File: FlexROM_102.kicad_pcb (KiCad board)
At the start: 2 copper layers, 16.5 x 34.3 mm, 7 parts, among them J1 27C256 DIP LEGS, U1 28C256

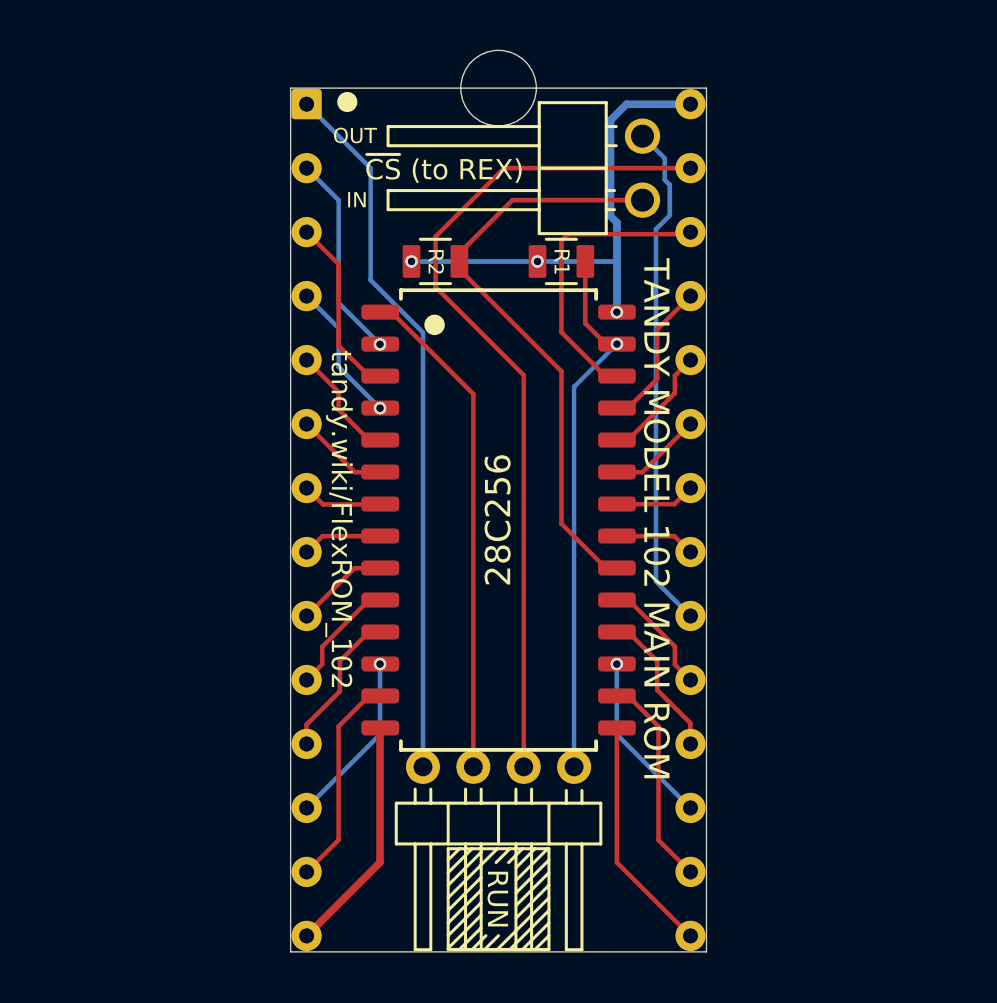
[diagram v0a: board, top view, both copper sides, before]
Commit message: add model 100 optrom programming adapter. readme and renders
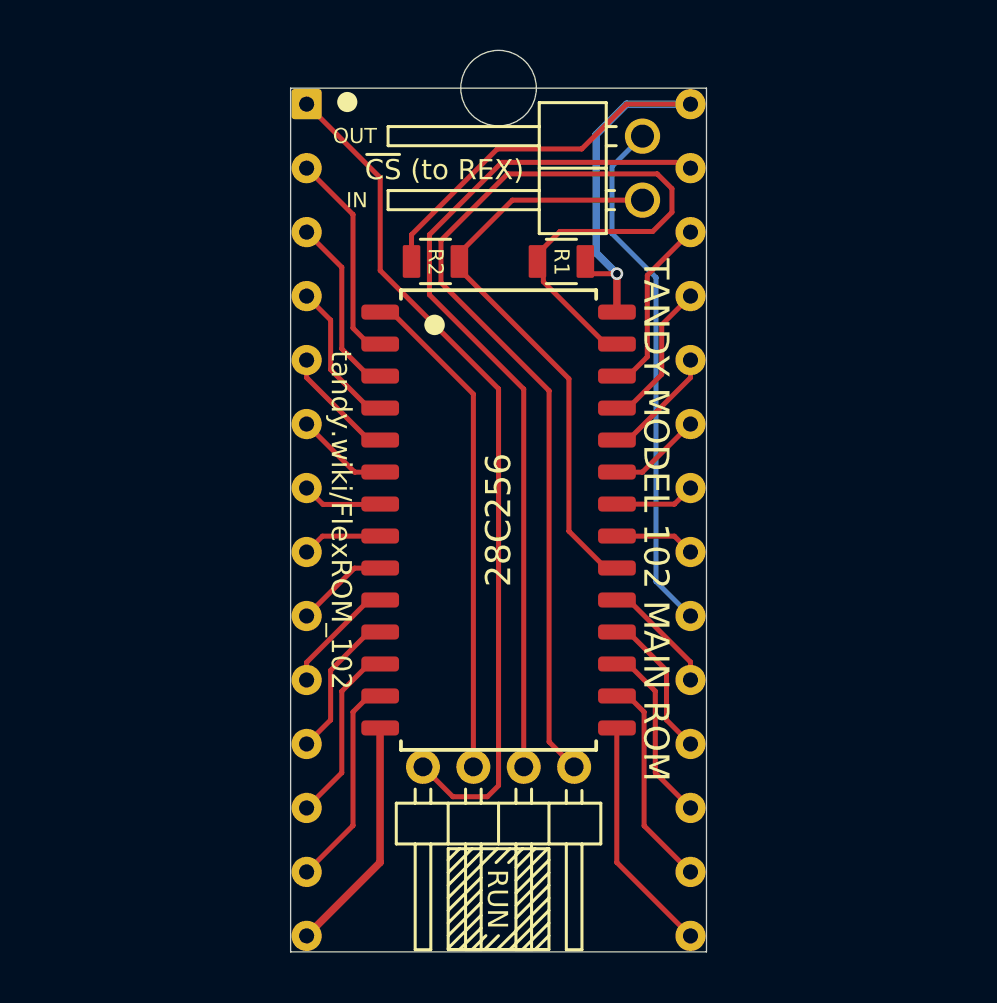
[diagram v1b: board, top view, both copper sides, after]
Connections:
- R1 pad 1: /~WE -> /VCC
- R1 pad 2: /VCC -> /~WE
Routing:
- net /~WE: track 21.6 -> 45.7 mm, vias 1 -> 0
- net /VCC: track 21.3 -> 27.7 mm, vias 3 -> 1
- net /NC_A14: track 28.2 -> 33.9 mm
- net /A13: track 11.8 -> 7.19 mm
- net /A14_~WE: track 33.8 -> 34.3 mm
- net /~CS_OUT: track 20.3 -> 20.8 mm
- net /D1: track 6.92 -> 7.18 mm, vias 1 -> 0
- net /D5: track 6.92 -> 7.18 mm, vias 1 -> 0
- net /A6: track 5.66 -> 5.91 mm, vias 1 -> 0
- net /A12: track 8.21 -> 8.45 mm, vias 1 -> 0

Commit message: add DS1000_DIP14
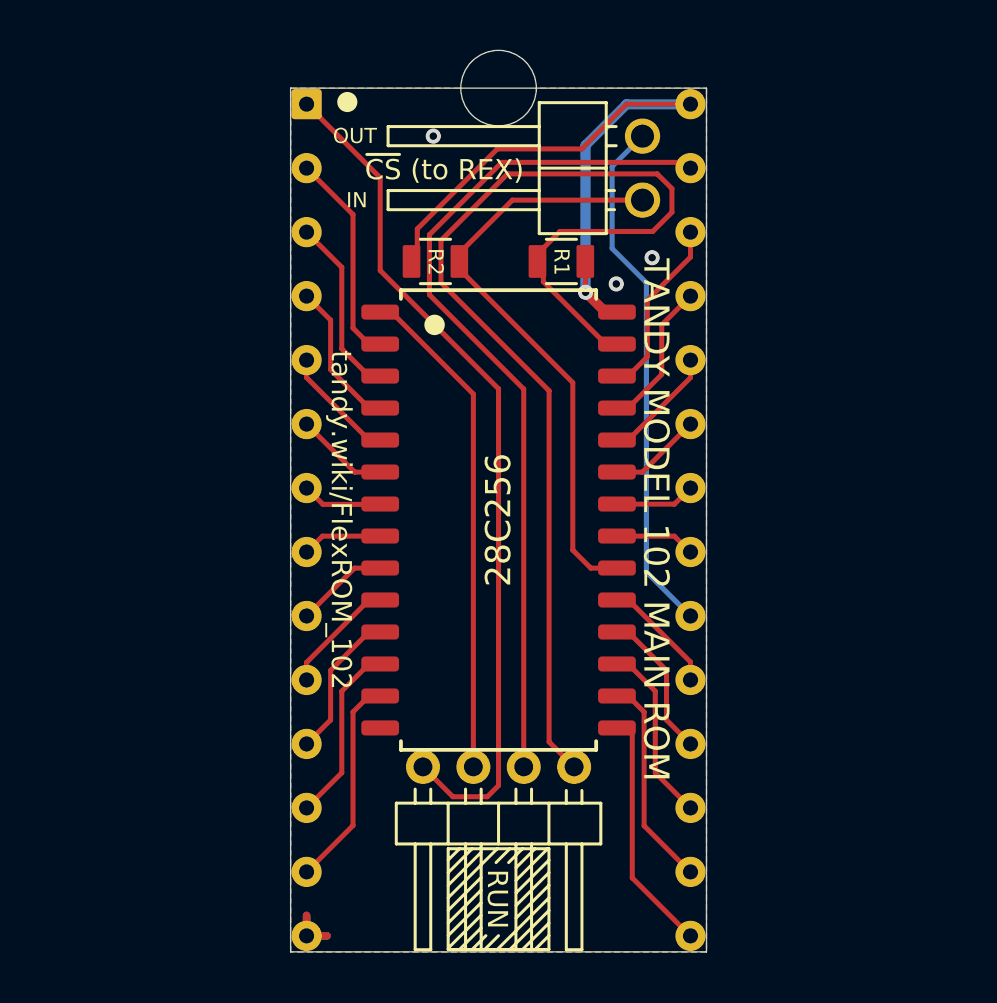
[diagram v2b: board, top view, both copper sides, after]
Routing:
- net /GND: track 9.46 -> 3.25 mm, vias 0 -> 3
- added copper zone on B.Cu, net /GND
- added copper zone on F.Cu, net /GND
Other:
- net class Default: clearance 0.16 -> 0.2; trace_width 0.18 -> 0.2; via_dia 0.5 -> 0.6
- rule trace_clearance: 0.16 -> 0.2
- rule trace_min: 0.16 -> 0.2

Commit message: kicad 6
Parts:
- JP1: value ~CS~ breakout (REX TP1) -> ~{CS} breakout (REX TP1)
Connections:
- net /A14_~WE renamed /A14_~{WE}
- net /~CS_IN renamed /~{CS_IN}
- net /~CS_OUT renamed /~{CS_OUT}
- net /~OE renamed /~{OE}
- net /~WE renamed /~{WE}
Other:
- net class Default removed
- board text added: "REX main rom: ~{CS} OUT to REX TP1 No REX: ~{CS} OUT to ~{CS} IN"
- board text added: "~{CS} (to REX)"
- board text removed: "REX main rom: ~CS~ OUT to REX TP1 No REX: ~CS~ OUT to ~CS~ IN"
- board text removed: "~CS~ (to REX)"

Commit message: FlexROM_102 outline, sch
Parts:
- removed REF**: NPTH_3mm, 000_LOCAL:NPTH_3mm
- J1: footprint 000_LOCAL:DIP28_0.6_pcb_sil_pins -> 000_LOCAL:DIP28_0.6_pcb
- moved JP1 19.7 mm to (114.3, 95.9), turned to -90 degrees
- moved R2 14.9 mm to (116.7, 104.1), turned to -90 degrees
- moved R1 14.9 mm to (116.7, 99.1), turned to -90 degrees
- moved JP2 14.5 mm to (136.8, 98.6), turned to 0 degrees
- turned J1 to 90 degrees
- turned U1 to 90 degrees
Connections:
- net /GND renamed GND
- net /VCC renamed VCC
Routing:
- net GND: track 3.25 -> 0.00 mm, vias 3 -> 0
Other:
- board size 16.5 x 34.3 mm -> 35.6 x 17.8 mm

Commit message: various minor cleanups
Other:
- board text added: "${TITLE} ${REVISION} ${COMMENT2}"
- board text added: "Boot from internal main rom: Connect ~{CS}_OUT to ~{CS}_IN Boot from REX_Classic main rom: Connect ~{CS}_OUT to REX TP1"
- board text added: "R1,R2: ${00000000-0000-0000-0000-00005f9fca43:VALUE} Legs: TE 1544210"
- board text removed: "Legs: TE 1544210"
- board text removed: "R1,R2: 47k"
- board text removed: "REX main rom: ~{CS} OUT to REX TP1 No REX: ~{CS} OUT to ~{CS} IN"
- board text removed: "To program: Set jumpers to PROGRAM. Put board in programmer. Set programmer for 28C256."
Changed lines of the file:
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@@
     (rev "005")
     (company "Brian K. White - b.kenyon.w@gmail.com")
+    (comment 2 "github.com/bkw777/aDIPters")
   )
   (layers
@@
   (gr_line (start 144.05 99.6) (end 140.05 99.6) (layer "F.SilkS") (width 0.12))
   (gr_line (start 140.5 103.6) (end 140.05 103.15) (layer "F.SilkS") (width 0.12))
-  (gr_text "R1,R2: 47k" (at 115.905 96.284 180) (layer "B.SilkS")
-    (effects (font (size 0.6 0.6) (thickness 0.08)) (justify left mirror))
-  )
-  (gr_text "Legs: TE 1544210" (at 115.905 95.395 180) (layer "B.SilkS")
+  (gr_text "R1,R2: ${00000000-0000-0000-0000-00005f9fca43:VALUE}\nLegs: TE 1544210" (at 144.145 107.315) (layer "B.SilkS")
     (effects (font (size 0.6 0.6) (thickness 0.08)) (justify left mirror))
   )
@@
     (effects (font (size 1 1) (thickness 0.15)) (justify mirror))
   )
+  (gr_text "${TITLE}  ${REVISION}\n${COMMENT2}" (at 127 96.52) (layer "B.SilkS")
+    (effects (font (size 0.8 0.8) (thickness 0.1)) (justify mirror))
+  )
   (gr_text "RUN" (at 135.1 101.6 90) (layer "B.SilkS")
     (effects (font (size 1 1) (thickness 0.15)) (justify mirror))
   )
-  (gr_text "To program:\n  Set jumpers to PROGRAM.\n  Put board in programmer.\n  Set programmer for 28C256." (at 110 101.6 180) (layer "B.SilkS")
-    (effects (font (size 1 1) (thickness 0.15)) (justify left mirror))
-  )
-  (gr_text "REX main rom: ~{CS} OUT to REX TP1\nNo REX: ~{CS} OUT to ~{CS} IN" (at 109.9 106.9 -180) (layer "B.SilkS")
-    (effects (font (size 1 1) (thickness 0.15)) (justify left mirror))
+  (gr_text "Boot from internal main rom:\nConnect ~{CS}_OUT to ~{CS}_IN\n\nBoot from REX_Classic main rom:\nConnect ~{CS}_OUT to REX TP1" (at 132.715 102.87) (layer "B.SilkS")
+    (effects (font (size 0.8 0.8) (thickness 0.1)) (justify left mirror))
   )
   (gr_text "tandy.wiki/FlexROM_102" (at 127 107.85) (layer "F.SilkS")
